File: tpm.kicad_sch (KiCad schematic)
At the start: 9 parts, among them J1001 PinHeader_2x7_P2mm_Drill0.9mm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, U1001 TS3A27518E_QFN

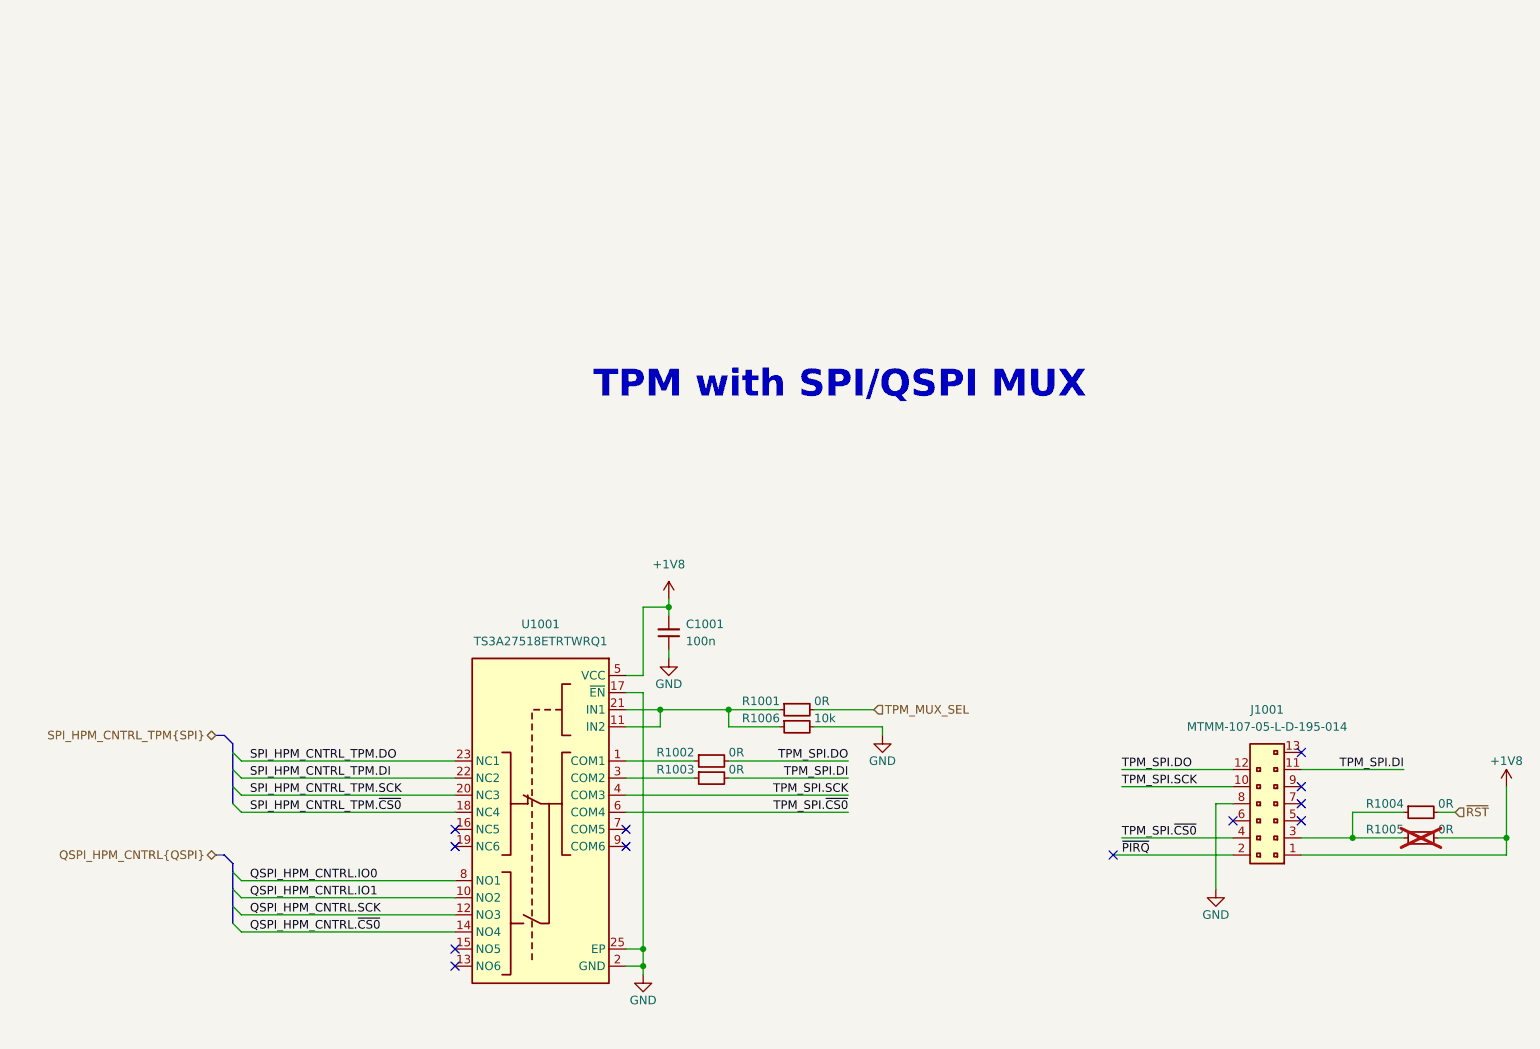
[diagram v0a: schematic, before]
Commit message: [#100501] Change TMP MUX with the same one as used for BIOS MUX, fix CS connection
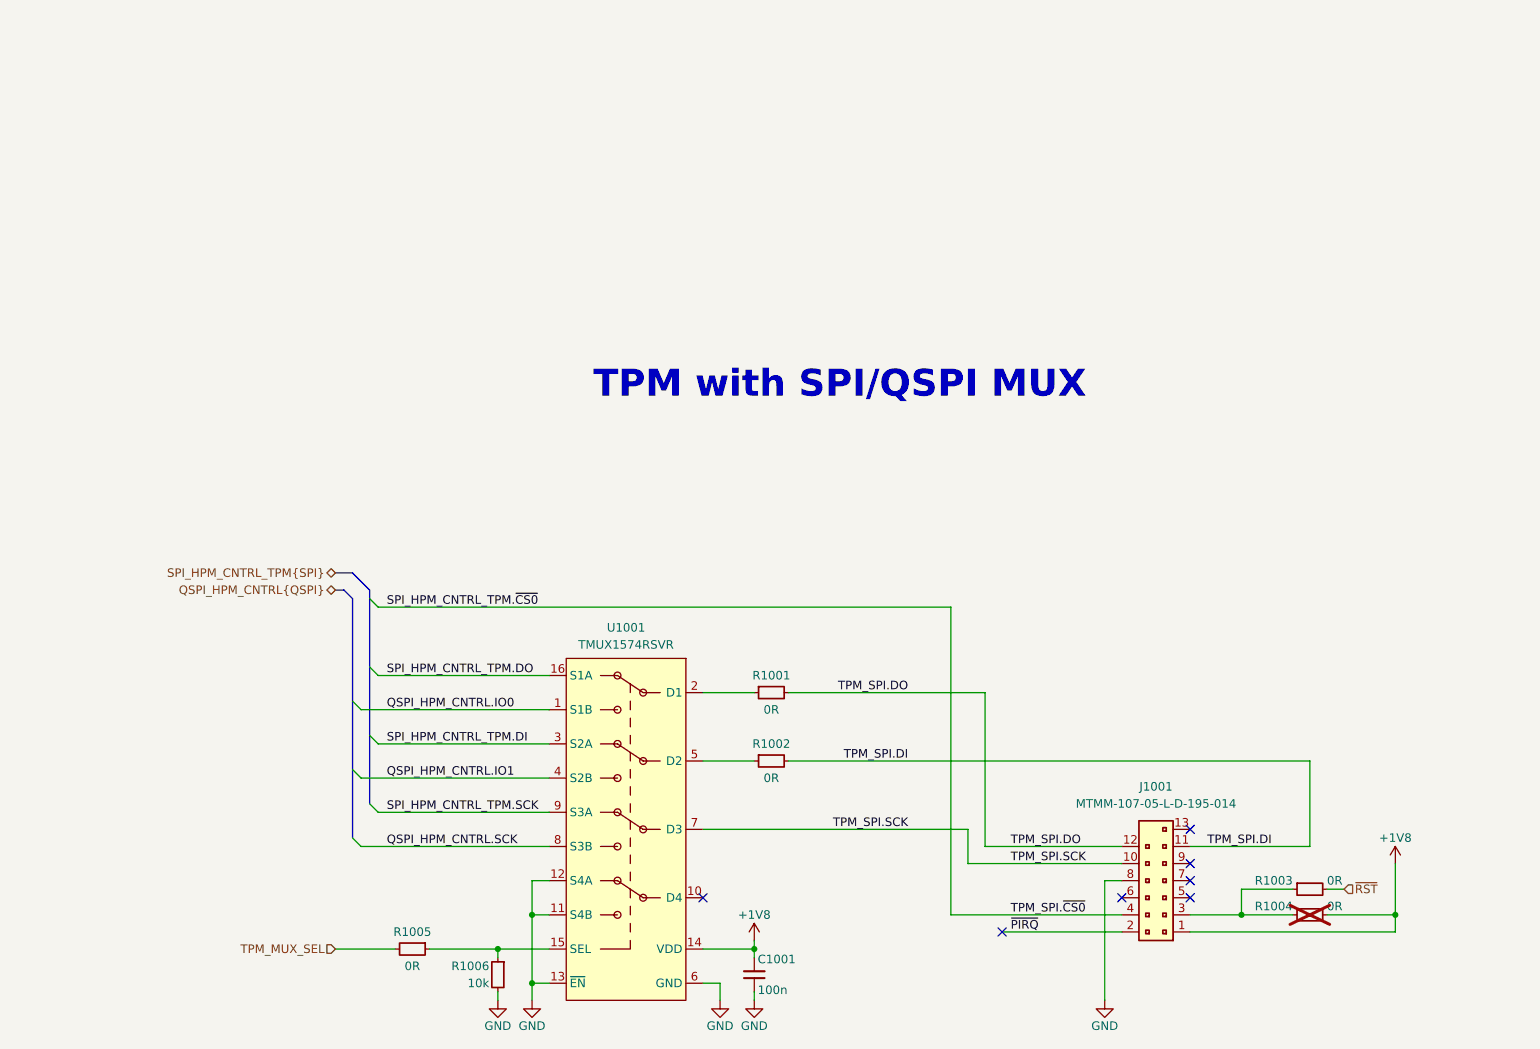
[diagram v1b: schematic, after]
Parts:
- removed U1001: TS3A27518E_QFN, antmicro-footprints:QFN-24-1EP_4x4mm_P0.5mm_EP2.6x2.6mm, symbol antmicroInterfaceAnalogSwitchesMultiplexersDemultiplexers:TS3A27518E_QFN
- added U1001: TMUX1574RSVR, antmicro-footprints:UQFN-16-1.8x2.6mm_P0.4mm_Texas_RSV0016A, symbol antmicroLogicSignalSwitchesMultiplexersDecoders:TMUX1574RSVR
- R1004: now not fitted; now left out of the parts list
- R1005: now fitted; now in the parts list
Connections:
- net TPM_SPI.~{CS0} is gone; now on net SPI_HPM_CNTRL_TPM.~{CS0}: J1001.4
- net +1V8: now also R1004.2, U1001.14 (VDD); no longer R1005.2
- net GND: now also U1001.11 (S4B), U1001.12 (S4A), U1001.13 (~{EN}), U1001.6 (GND)
- net QSPI_HPM_CNTRL.IO0: now also U1001.1 (S1B)
- net QSPI_HPM_CNTRL.IO1: now also U1001.4 (S2B)
- net QSPI_HPM_CNTRL.SCK: now also U1001.8 (S3B)
- net SPI_HPM_CNTRL_TPM.DI: now also U1001.3 (S2A)
- net SPI_HPM_CNTRL_TPM.DO: now also U1001.16 (S1A)
- net SPI_HPM_CNTRL_TPM.SCK: now also U1001.9 (S3A)
- net TPM_MUX_SEL: now also R1005.2; no longer R1001.2
- net TPM_SPI.DI: now also R1002.2; no longer R1003.2
- net TPM_SPI.DO: now also R1001.2; no longer R1002.2
- net TPM_SPI.SCK: now also U1001.7 (D3)
- net ~{RST}: now also R1003.2; no longer R1004.2
- net at J1001.3, R1004.1: now also R1003.1; no longer R1005.1
- net at R1002.1: now also U1001.5 (D2)
- net at R1006.1: now also R1005.1, U1001.15 (SEL); no longer R1001.1
- new net: R1001.1, U1001.2 (D1)
- no-connect marks 12 -> 7

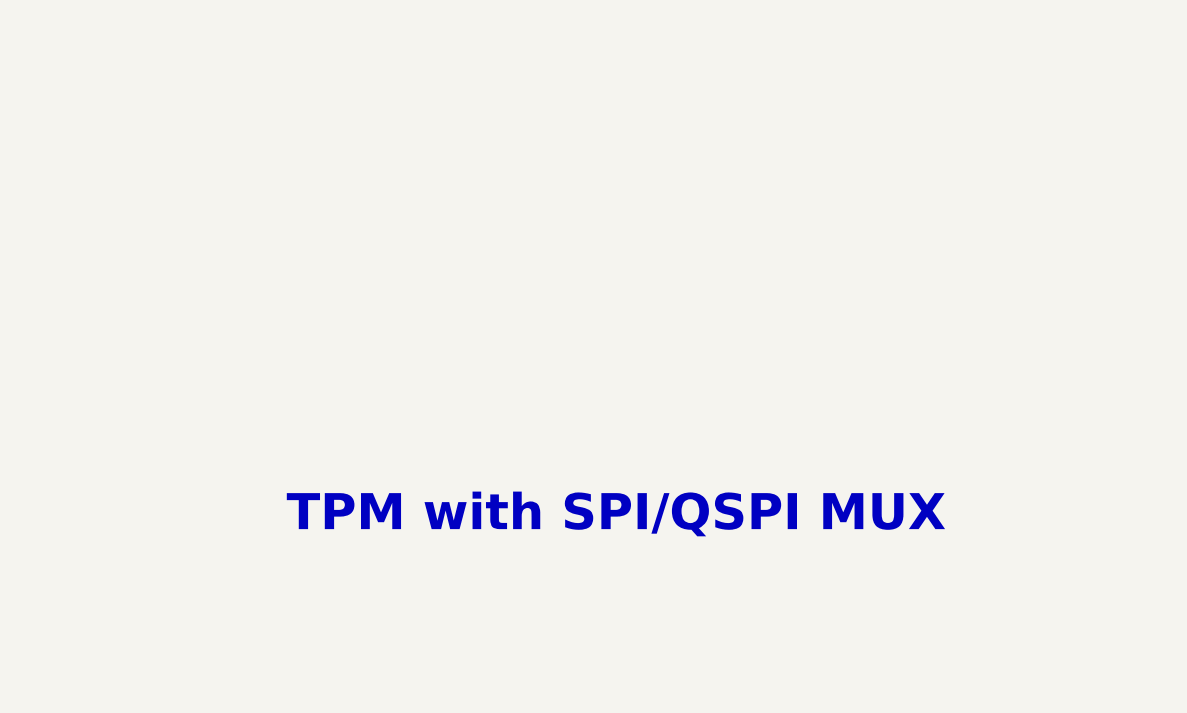
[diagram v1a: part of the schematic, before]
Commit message: [#100282] Add missing schematic sheet names and align them all
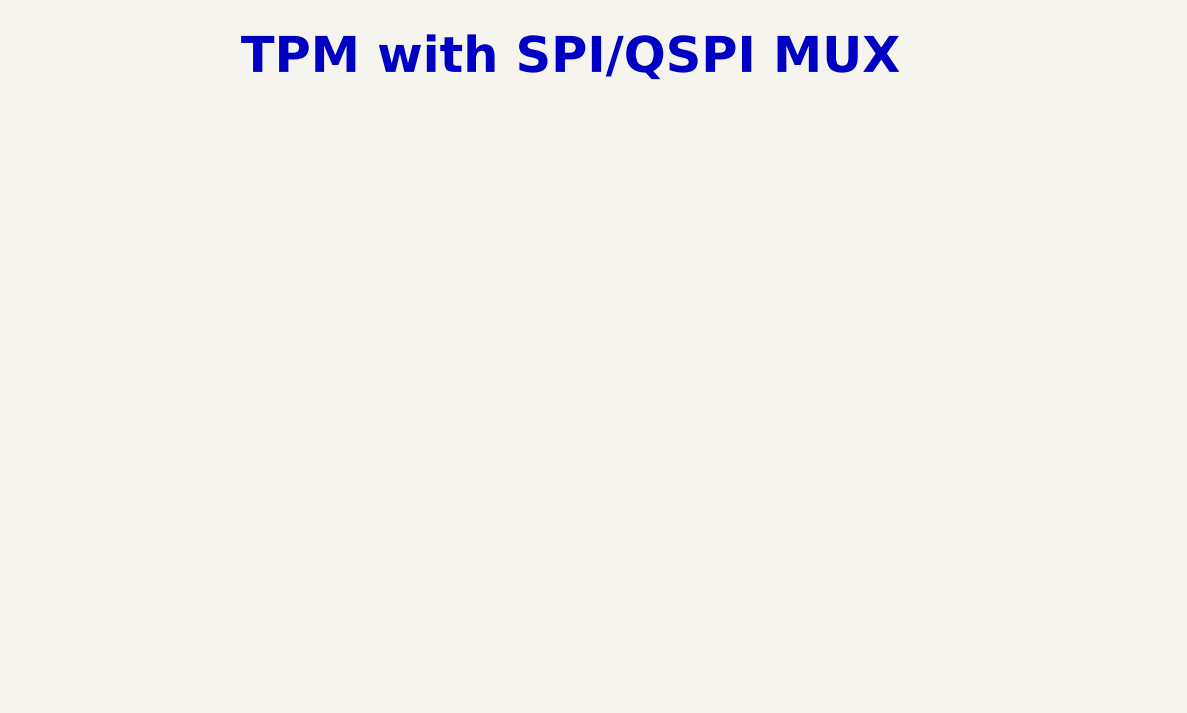
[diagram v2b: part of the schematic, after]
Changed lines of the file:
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@@
 	(text "TPM with SPI/QSPI MUX"
 		(exclude_from_sim no)
-		(at 215.9 88.9 0)
+		(at 210.82 38.1 0)
 		(effects
 			(font

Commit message: [#100501] Reannotate schematic
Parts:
- renumbered C1001 to C83, J1001 to J4, R1001 to R100, R1002 to R101, R1003 to R102, R1004 to R103, R1005 to R104, R1006 to R105, U1001 to U11
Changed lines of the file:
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@@
 		(in_pos_files yes)
 		(dnp no)
-		(property "Reference" "#PWR01002"
+		(property "Reference" "#PWR0121"
 			(at 218.44 173.99 0)
 			(hide yes)
@@
 			(project "altera-modular-agilex-5-dc-scm"
 				(path "/6bb9d978-a328-4b30-874b-55170a976185/af45e011-8332-484c-9b46-08bd6b2c8877"
-					(reference "#PWR01002")
+					(reference "#PWR0121")
 					(unit 1)
 				)
@@
 		(in_pos_files yes)
 		(dnp no)
-		(property "Reference" "#PWR01006"
+		(property "Reference" "#PWR0125"
 			(at 194.31 182.88 0)
 			(hide yes)
@@
 			(project "altera-modular-agilex-5-dc-scm"
 				(path "/6bb9d978-a328-4b30-874b-55170a976185/af45e011-8332-484c-9b46-08bd6b2c8877"
-					(reference "#PWR01006")
+					(reference "#PWR0125")
 					(unit 1)
 				)
@@
 		(in_pos_files yes)
 		(dnp no)
-		(property "Reference" "R1005"
+		(property "Reference" "R104"
 			(at 152.4 170.18 0)
 			(show_name no)
@@
 			(project "altera-modular-agilex-5-dc-scm"
 				(path "/6bb9d978-a328-4b30-874b-55170a976185/af45e011-8332-484c-9b46-08bd6b2c8877"
-					(reference "R1005")
+					(reference "R104")
 					(unit 1)
 				)
@@
 		(in_pos_files yes)
 		(dnp no)
-		(property "Reference" "#PWR01005"
+		(property "Reference" "#PWR0124"
 			(at 189.23 182.88 0)
 			(hide yes)
@@
 			(project "altera-modular-agilex-5-dc-scm"
 				(path "/6bb9d978-a328-4b30-874b-55170a976185/af45e011-8332-484c-9b46-08bd6b2c8877"
-					(reference "#PWR01005")
+					(reference "#PWR0124")
 					(unit 1)
 				)
@@
 		(in_pos_files yes)
 		(dnp no)
-		(property "Reference" "R1001"
+		(property "Reference" "R100"
 			(at 205.74 132.08 0)
 			(show_name no)
@@
 			(project "altera-modular-agilex-5-dc-scm"
 				(path "/6bb9d978-a328-4b30-874b-55170a976185/af45e011-8332-484c-9b46-08bd6b2c8877"
-					(reference "R1001")
+					(reference "R100")
 					(unit 1)
 				)
@@
 		(in_pos_files yes)
 		(dnp yes)
-		(property "Reference" "R1004"
+		(property "Reference" "R103"
 			(at 283.21 166.37 0)
 			(show_name no)
@@
 			(project "altera-modular-agilex-5-dc-scm"
 				(path "/6bb9d978-a328-4b30-874b-55170a976185/af45e011-8332-484c-9b46-08bd6b2c8877"
-					(reference "R1004")
+					(reference "R103")
 					(unit 1)
 				)
@@
 		(in_pos_files yes)
 		(dnp no)
-		(property "Reference" "R1002"
+		(property "Reference" "R101"
 			(at 205.74 142.24 0)
 			(show_name no)
@@
 			(project "altera-modular-agilex-5-dc-scm"
 				(path "/6bb9d978-a328-4b30-874b-55170a976185/af45e011-8332-484c-9b46-08bd6b2c8877"
-					(reference "R1002")
+					(reference "R101")
 					(unit 1)
 				)
@@
 		(in_pos_files yes)
 		(dnp no)
-		(property "Reference" "#PWR01007"
+		(property "Reference" "#PWR0126"
 			(at 264.16 182.88 0)
 			(hide yes)
@@
 			(project "altera-modular-agilex-5-dc-scm"
 				(path "/6bb9d978-a328-4b30-874b-55170a976185/af45e011-8332-484c-9b46-08bd6b2c8877"
-					(reference "#PWR01007")
+					(reference "#PWR0126")
 					(unit 1)
 				)
@@
 		(in_pos_files yes)
 		(dnp no)
-		(property "Reference" "U1001"
+		(property "Reference" "U11"
 			(at 184.15 124.968 0)
 			(show_name no)
@@
 			(project "altera-modular-agilex-5-dc-scm"
 				(path "/6bb9d978-a328-4b30-874b-55170a976185/af45e011-8332-484c-9b46-08bd6b2c8877"
-					(reference "U1001")
+					(reference "U11")
 					(unit 1)
 				)
@@
 		(in_pos_files yes)
 		(dnp no)
-		(property "Reference" "R1003"
+		(property "Reference" "R102"
 			(at 283.21 162.56 0)
 			(show_name no)
@@
 			(project "altera-modular-agilex-5-dc-scm"
 				(path "/6bb9d978-a328-4b30-874b-55170a976185/af45e011-8332-484c-9b46-08bd6b2c8877"
-					(reference "R1003")
+					(reference "R102")
 					(unit 1)
 				)
@@
 		(in_pos_files yes)
 		(dnp no)
-		(property "Reference" "#PWR01004"
+		(property "Reference" "#PWR0123"
 			(at 161.29 182.88 0)
 			(hide yes)
@@
 			(project "altera-modular-agilex-5-dc-scm"
 				(path "/6bb9d978-a328-4b30-874b-55170a976185/af45e011-8332-484c-9b46-08bd6b2c8877"
-					(reference "#PWR01004")
+					(reference "#PWR0123")
 					(unit 1)
 				)
@@
 		(in_pos_files yes)
 		(dnp no)
-		(property "Reference" "#PWR01003"
+		(property "Reference" "#PWR0122"
 			(at 173.99 182.88 0)
 			(hide yes)
@@
 			(project "altera-modular-agilex-5-dc-scm"
 				(path "/6bb9d978-a328-4b30-874b-55170a976185/af45e011-8332-484c-9b46-08bd6b2c8877"
-					(reference "#PWR01003")
+					(reference "#PWR0122")
 					(unit 1)
 				)
@@
 		(in_pos_files yes)
 		(dnp no)
-		(property "Reference" "R1006"
+		(property "Reference" "R105"
 			(at 163.83 175.26 90)
 			(show_name no)
@@
 			(project "altera-modular-agilex-5-dc-scm"
 				(path "/6bb9d978-a328-4b30-874b-55170a976185/af45e011-8332-484c-9b46-08bd6b2c8877"
-					(reference "R1006")
+					(reference "R105")
 					(unit 1)
 				)
@@
 		(in_pos_files yes)
 		(dnp no)
-		(property "Reference" "#PWR01001"
+		(property "Reference" "#PWR0120"
 			(at 313.69 162.56 0)
 			(hide yes)
@@
 			(project "altera-modular-agilex-5-dc-scm"
 				(path "/6bb9d978-a328-4b30-874b-55170a976185/af45e011-8332-484c-9b46-08bd6b2c8877"
-					(reference "#PWR01001")
+					(reference "#PWR0120")
 					(unit 1)
 				)
@@
 		(dnp no)
 		(fields_autoplaced yes)
-		(property "Reference" "J1001"
+		(property "Reference" "J4"
 			(at 262.89 148.59 0)
 			(show_name no)
@@
 			(project "altera-modular-agilex-5-dc-scm"
 				(path "/6bb9d978-a328-4b30-874b-55170a976185/af45e011-8332-484c-9b46-08bd6b2c8877"
-					(reference "J1001")
+					(reference "J4")
 					(unit 1)
 				)
@@
 		(in_pos_files yes)
 		(dnp no)
-		(property "Reference" "C1001"
+		(property "Reference" "C83"
 			(at 203.708 174.244 90)
 			(show_name no)
@@
 			(project "altera-modular-agilex-5-dc-scm"
 				(path "/6bb9d978-a328-4b30-874b-55170a976185/af45e011-8332-484c-9b46-08bd6b2c8877"
-					(reference "C1001")
+					(reference "C83")
 					(unit 1)
 				)

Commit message: [#100501] Clean ERC
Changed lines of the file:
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@@
-		)
-	)
-	(label "TPM_SPI.~{CS0}"
-		(at 241.3 167.64 0)
-		(effects
-			(font
-				(size 1.27 1.27)
-			)
-			(justify left bottom)
 		)
 	)
